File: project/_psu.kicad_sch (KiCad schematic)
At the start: 43 parts, among them J201 24V, J202 5V, J203 3V3, J204 6V, Q201 MMBT3904, U201 LW6550A23E, U202 MT3406, U203 ME3121AM6G

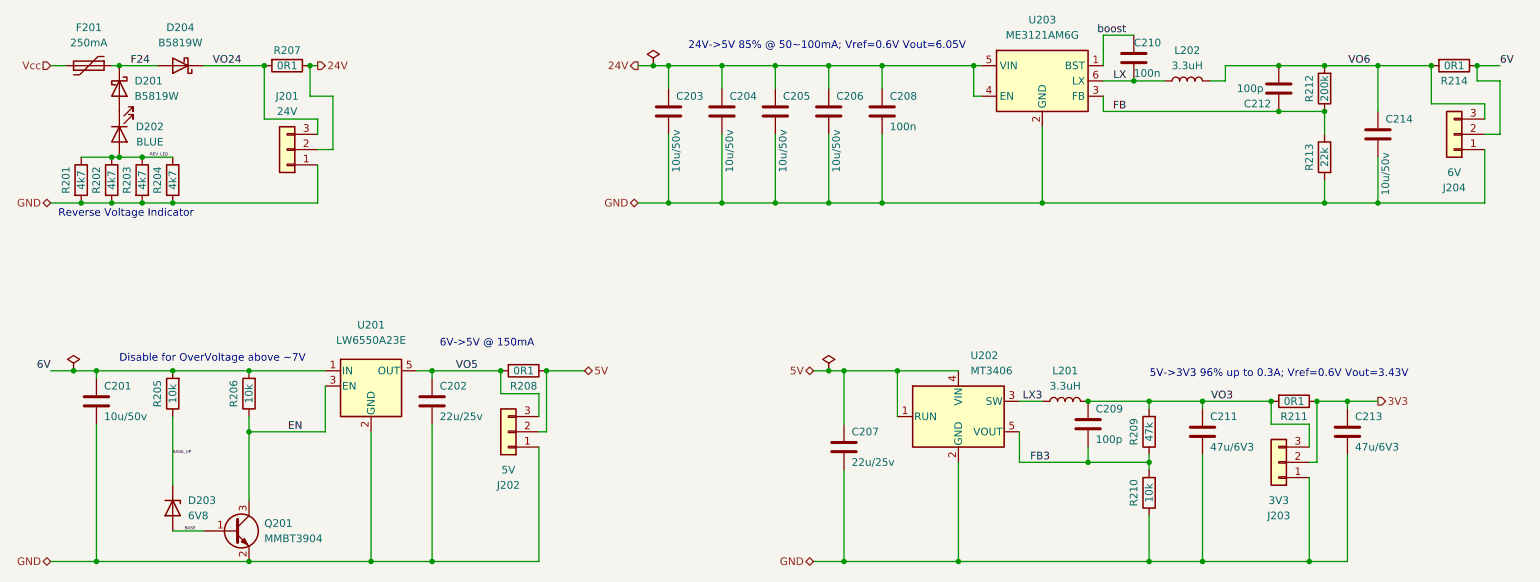
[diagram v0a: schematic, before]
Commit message: fixes after preliminary testing
* Switching to TMP102 as TMP101 is no longer available
* Removing 5V LDO with OVP as it caused more problems
* bumping up version
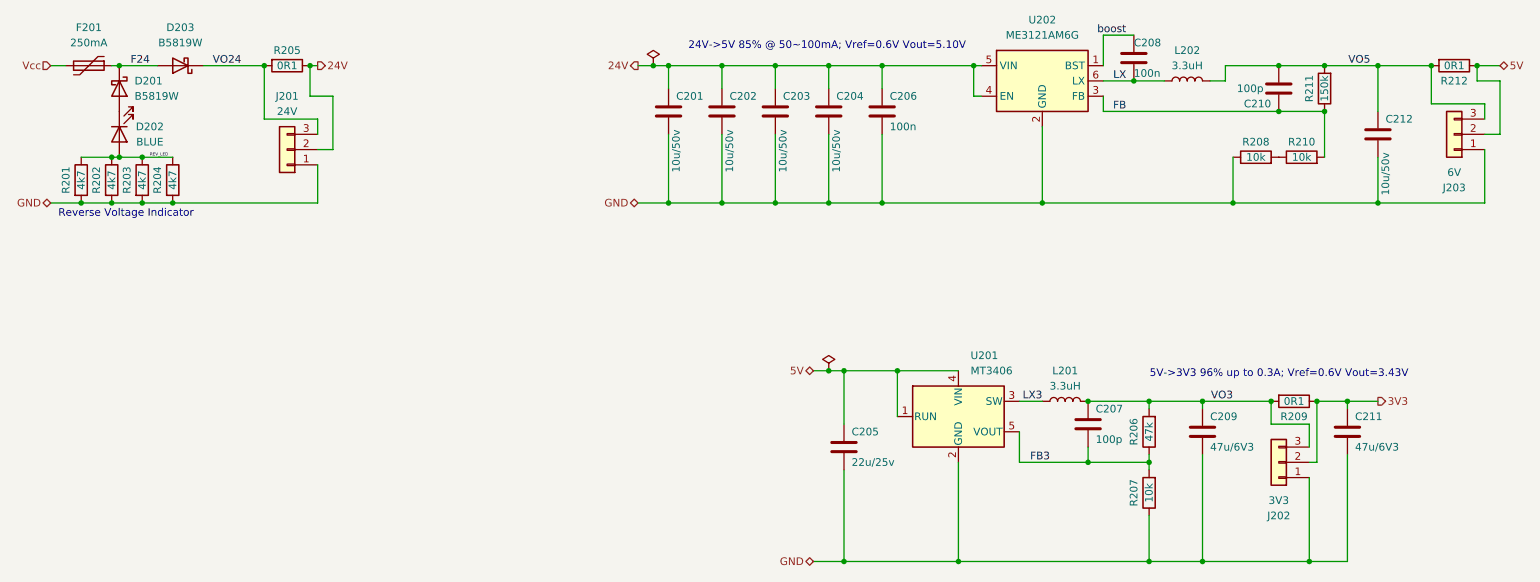
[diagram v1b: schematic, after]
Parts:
- removed C201: 10u/50v, Capacitor_SMD:C_0805_2012Metric_Pad1.18x1.45mm_HandSolder, symbol Device:C
- removed C202: 22u/25v, Capacitor_SMD:C_0805_2012Metric_Pad1.18x1.45mm_HandSolder, symbol Device:C
- removed D203: 6V8, Diode_SMD:D_SOD-323_HandSoldering, symbol Device:D_Zener
- removed J202: 5V, Connector_PinHeader_2.54mm:PinHeader_1x03_P2.54mm_Vertical, symbol Connector_Generic:Conn_01x03
- removed Q201: MMBT3904, Package_TO_SOT_SMD:SOT-23, symbol Device:Q_NPN_BEC
- removed R205, R206: 10k, Resistor_SMD:R_0805_2012Metric_Pad1.20x1.40mm_HandSolder, symbol Device:R
- removed R213: 22k, Resistor_SMD:R_0805_2012Metric_Pad1.20x1.40mm_HandSolder, symbol Device:R
- removed U201: LW6550A23E, Package_TO_SOT_SMD:SOT-23-5, symbol Regulator_Linear:TLV71209_SOT23-5
- added R210: 10k, Resistor_SMD:R_0805_2012Metric_Pad1.20x1.40mm_HandSolder, symbol Device:R
- R208: value 0R1 -> 10k; jlc-part-type E -> B; lcsc# C127687 -> C17414
- R211: renamed from R212; value 200k -> 150k; lcsc# C17539 -> C17470
- renumbered C203 to C201, C204 to C202, C205 to C203, C206 to C204, C207 to C205, C208 to C206, C209 to C207, C210 to C208, C211 to C209, C212 to C210, C213 to C211, C214 to C212, D204 to D203, J203 to J202, J204 to J203, R207 to R205, R209 to R206, R210 to R207, R211 to R209, R214 to R212, U202 to U201, U203 to U202
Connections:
- net 6V is gone; now on net 5V: J203.2 (Pin_2), R212.1
- net VO6 is gone; now on net VO5: C210.2, C212.1, J203.3 (Pin_3), L202.2, R211.2, R212.2
- net 5V: no longer R208.1
- net FB: now also R210.2
- net GND: now also R208.1
- net VO5: no longer R208.2
- new net: R208.2, R210.1
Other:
- note added: "24V->5V 85% @ 50~100mA; Vref=0.6V Vout=5.10V"
- note removed: "24V->5V 85% @ 50~100mA; Vref=0.6V Vout=6.05V"
- note removed: "6V->5V @ 150mA"
- note removed: "Disable for OverVoltage above ~7V"
